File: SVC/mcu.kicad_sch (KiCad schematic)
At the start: 26 parts, among them J11 629722000214, J12 AVR-ISP-6, M1 Fan_4pin, SW1 SW_Push, U14 ATmega32U4-A

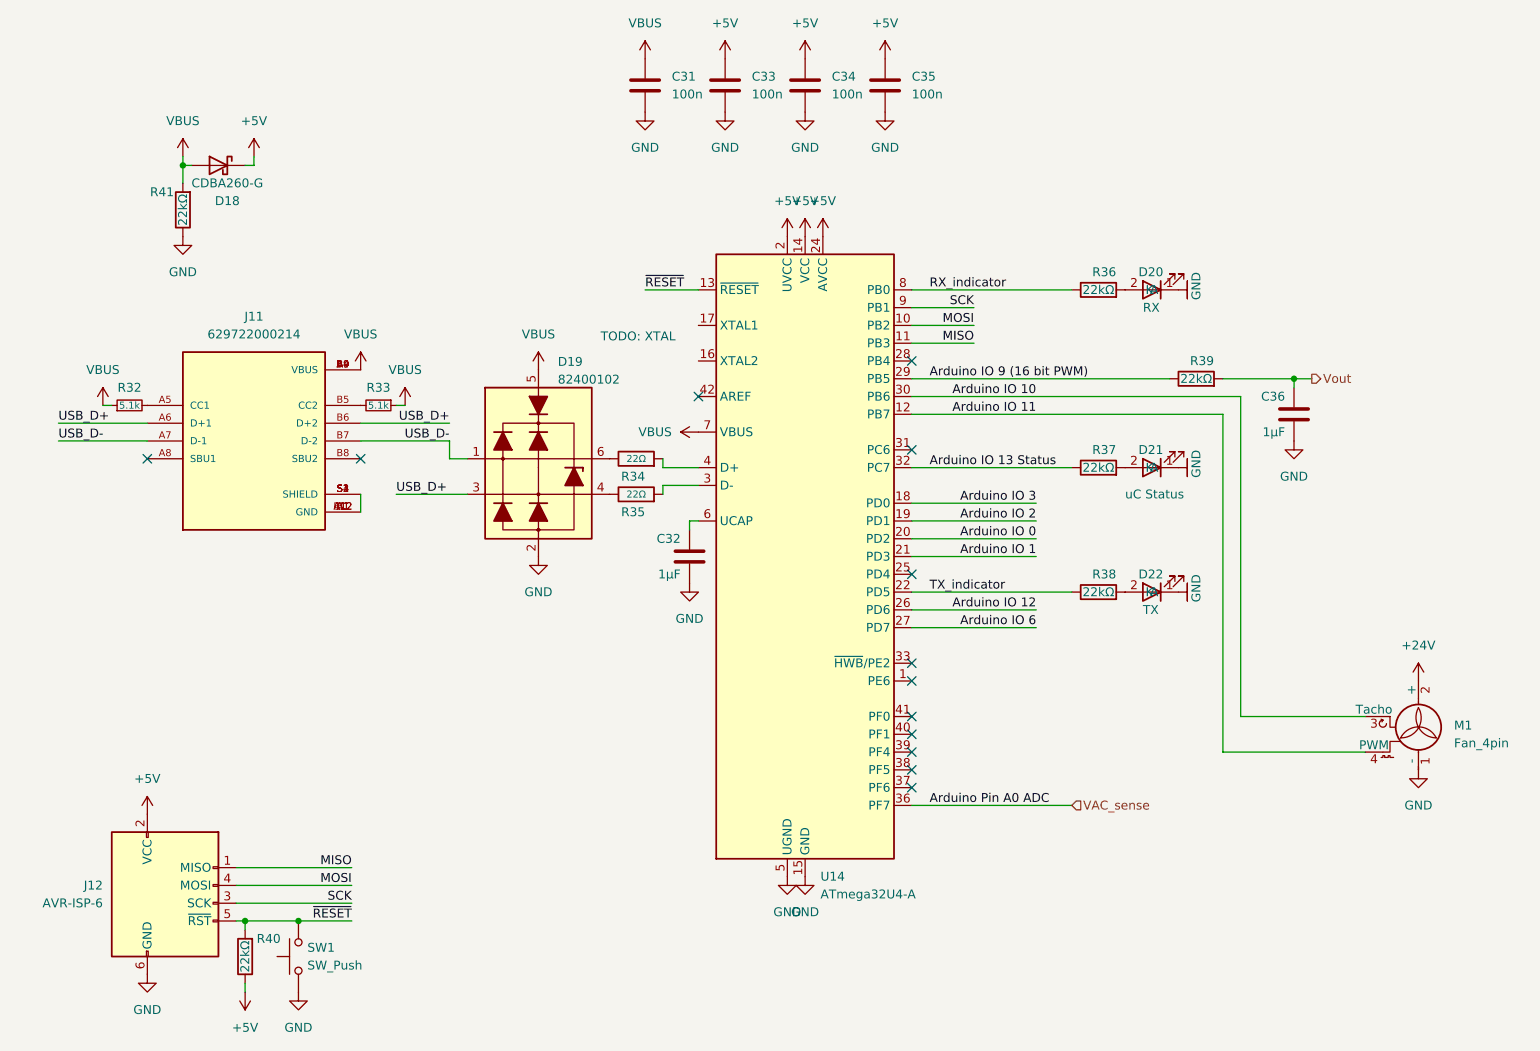
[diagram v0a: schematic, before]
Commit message: did some layout work, minor schematic changes to help with layout
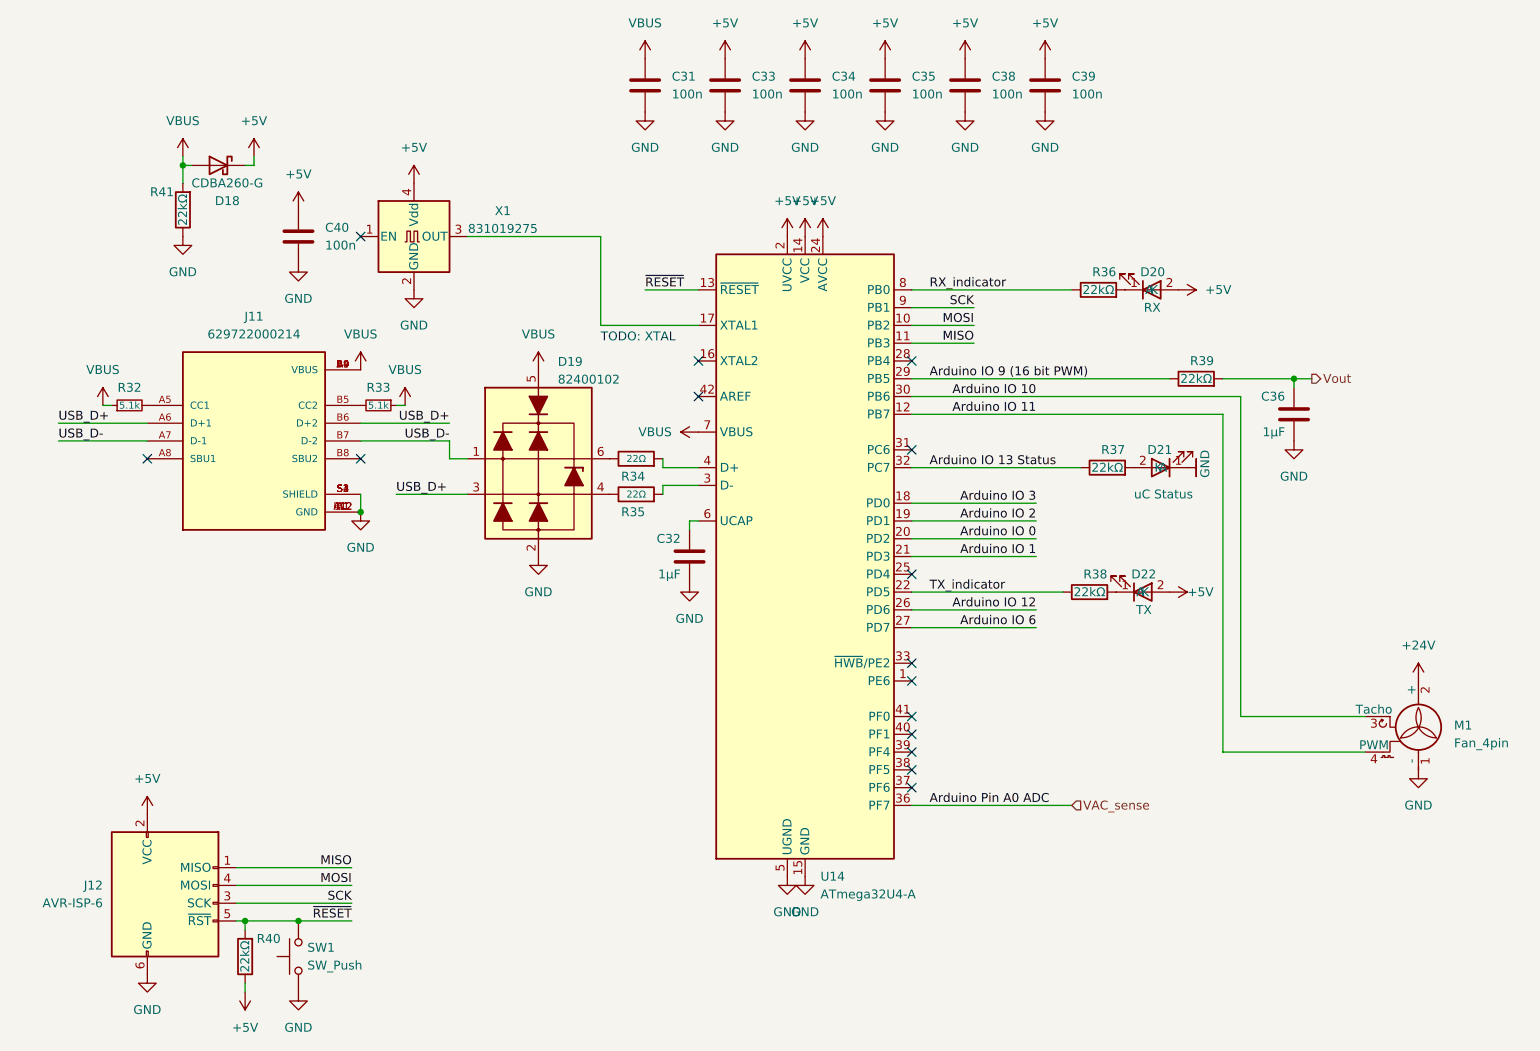
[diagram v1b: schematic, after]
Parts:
- added C38, C39, C40: 100n, Capacitor_SMD:C_0805_2012Metric, symbol Device:C
- added X1: 831019275, Oscillator:Oscillator_SMD_Abracon_ASV-4Pin_7.0x5.1mm, symbol Oscillator:ASV-xxxMHz
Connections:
- net +5V: now also D20.2 (A), D22.2 (A), C38.1, C39.1, C40.1, X1.4 (Vdd)
- net GND: now also J11.A1 (GND), J11.A12 (GND), J11.B1 (GND), J11.B12 (GND), J11.S1 (SHIELD), J11.S2 (SHIELD), J11.S3 (SHIELD), J11.S4 (SHIELD), C38.2, C39.2, C40.2, X1.2 (GND); no longer D20.1 (K), D22.1 (K)
- net at R38.2: now also D22.1 (K); no longer D22.2 (A)
- net at R36.2: now also D20.1 (K); no longer D20.2 (A)
- net at U14.17 (XTAL1): now also X1.3 (OUT)
- no-connect marks 13 -> 15
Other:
- moved on the sheet: D20, D21, D22, R37, R38
